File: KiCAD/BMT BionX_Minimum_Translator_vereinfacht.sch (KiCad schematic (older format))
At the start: 30 parts, among them J1 Kunteng Display Connector, J2 SAE Power Connector Motor, J3 Rosenberg Motor, J4 External BB Torquesensor, J5 Brake connector, J6 Throttle connector, J7 CAN Connector, J9 Batterieanschluß, Q1 IRF3205, Q2 IRF3205, U1 BP, U2 MCP2551-CAN Transceiver, U3 VOM1271, U4 SD12-5, U5 VOM1271

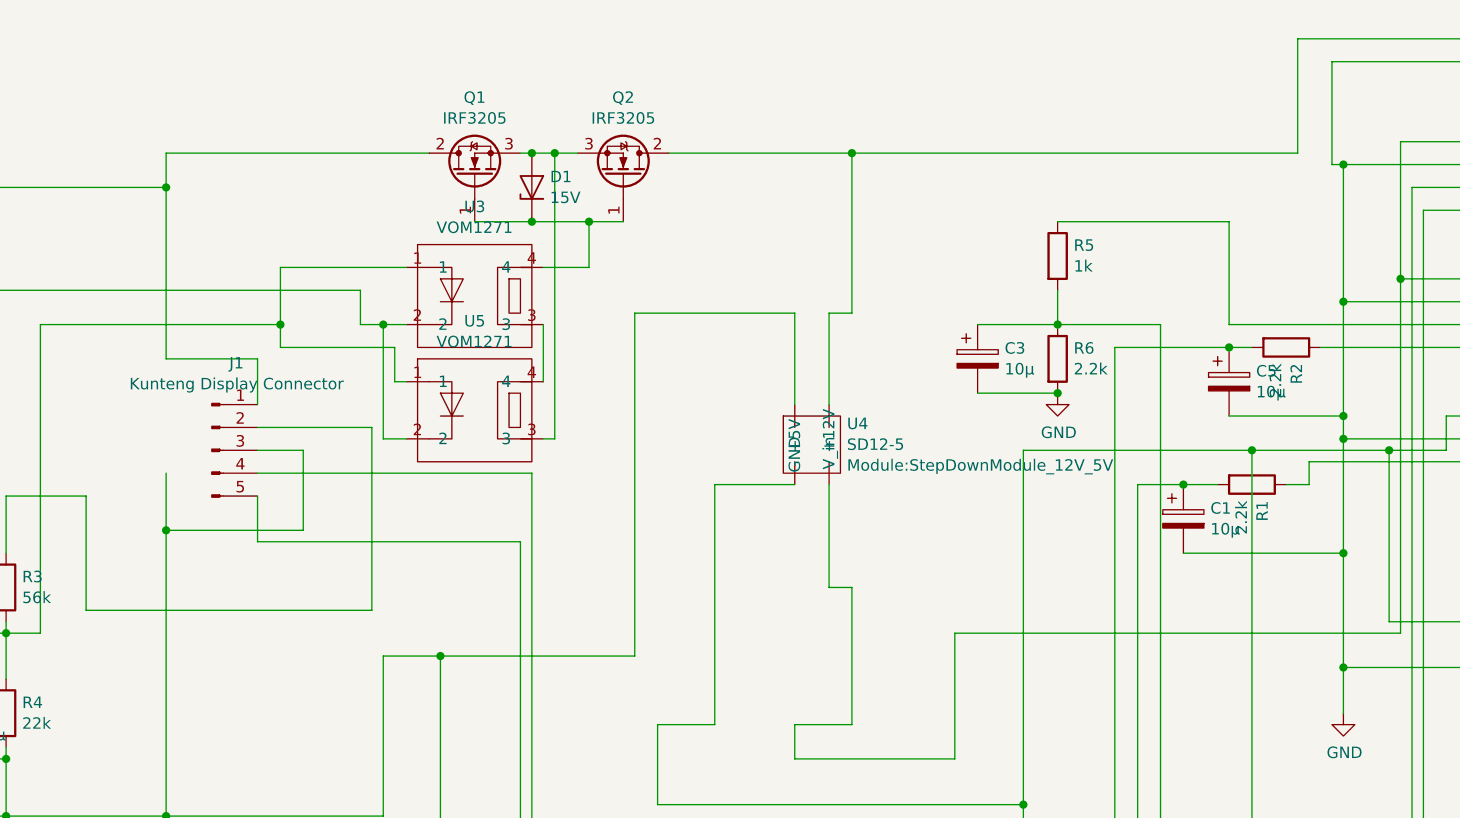
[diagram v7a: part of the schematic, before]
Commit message: Step Down switched seperately
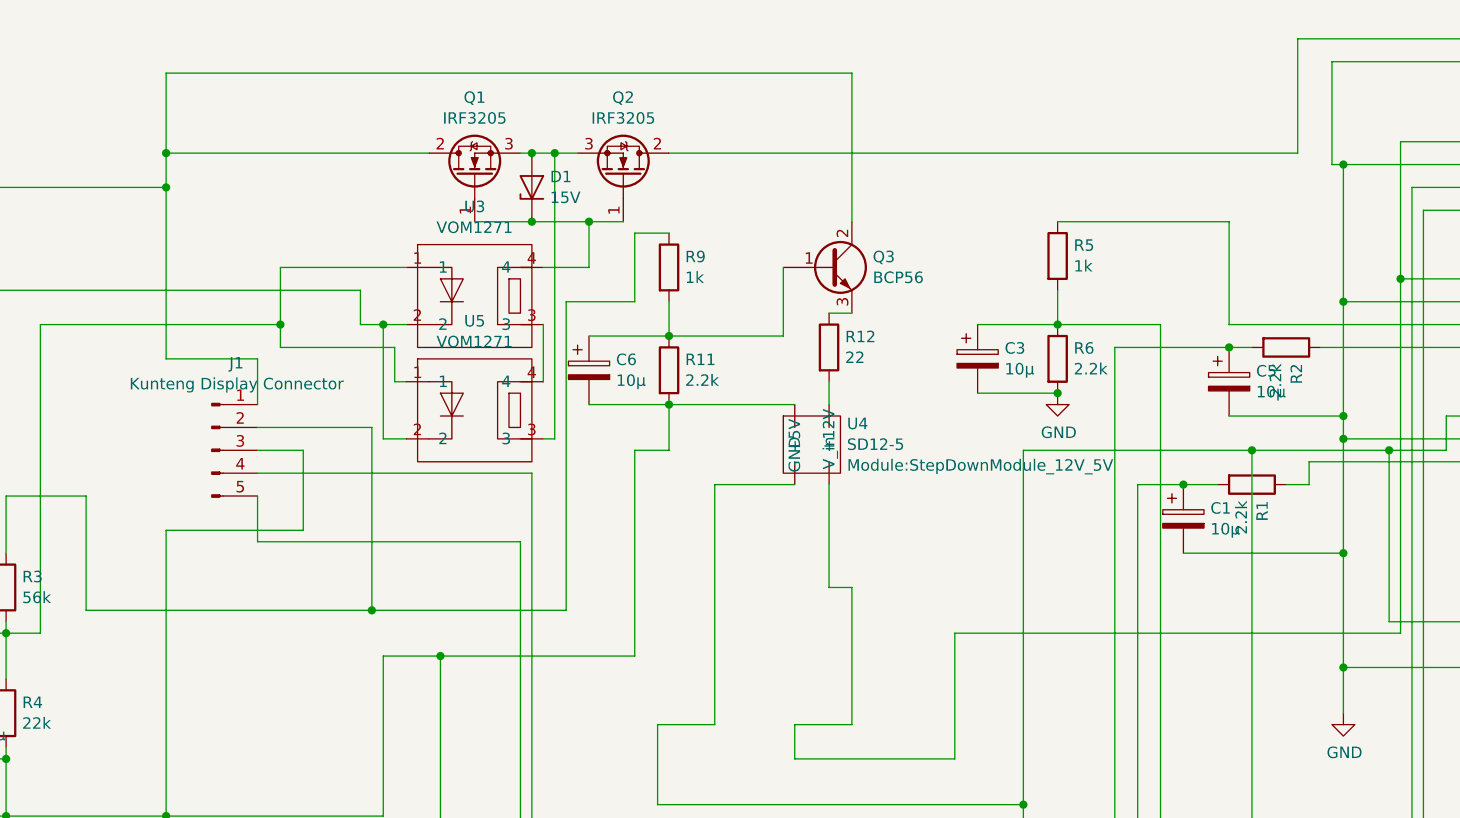
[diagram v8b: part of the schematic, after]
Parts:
- added C6: 10µ, Capacitor_THT:CP_Radial_D5.0mm_P2.50mm, symbol Device:CP
- added Q3: BCP56, Package_TO_SOT_SMD:SOT-223, symbol Transistor_BJT:BCP56
- added R11: 2.2k, Resistor_SMD:R_0805_2012Metric, symbol Device:R
- added R12: 22, Resistor_SMD:R_0805_2012Metric, symbol Device:R
- added R9: 1k, Resistor_SMD:R_0805_2012Metric, symbol Device:R
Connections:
- net +BATT: now also Q3.2 (C), Q3.4 (C)
- net GND: now also C6.2, R11.2
- net at J1.2 (Pin_2), R3.1: now also R9.1
- net at J2.1 (Pin_1), Q2.2 (D): no longer U4.V_in
- new net: C6.1, Q3.1 (B), R11.1, R9.2
- new net: Q3.3 (E), R12.1
- new net: R12.2, U4.V_in
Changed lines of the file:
@@
 $EndComp
-Wire Wire Line
-	4950 1450 5750 1450
-Connection ~ 5750 1450
-Wire Wire Line
-	5750 1450 7700 1450
-Wire Wire Line
-	5750 1450 5750 2150
 Wire Wire Line
 	6200 3550 6200 4100
@@
 Wire Wire Line
 	3950 3650 4800 3650
-Wire Wire Line
-	4800 3650 4800 2150
 Connection ~ 3950 3650
 $Comp
@@
 $EndComp
 Wire Wire Line
-	5500 2150 5500 2550
-Wire Wire Line
-	4800 2150 5500 2150
-Wire Wire Line
 	5750 2150 5650 2150
-Wire Wire Line
-	5650 2150 5650 2550
 Wire Wire Line
 	5650 2900 5650 3350
@@
 Wire Wire Line
 	3350 2750 3150 2750
-Connection ~ 2750 3100
-Wire Wire Line
-	2750 3100 2750 2850
 Wire Wire Line
 	3350 2750 3350 3100
@@
 Wire Wire Line
 	2750 1450 3900 1450
+Wire Wire Line
+	4950 1450 7700 1450
+$Comp
+L Transistor_BJT:BCP56 Q3
+U 1 1 5F8B6DF6
+P 5650 1950
+F 0 "Q3" H 5841 1996 50  0000 L CNN
+F 1 "BCP56" H 5841 1905 50  0000 L CNN
+F 2 "Package_TO_SOT_SMD:SOT-223" H 5850 1875 50  0001 L CIN
+F 3 "http://cache.nxp.com/documents/data_sheet/BCP56_BCX56_BC56PA.pdf?pspll=1" H 5650 1950 50  0001 L CNN
+	1    5650 1950
+	1    0    0    -1
+$EndComp
+Wire Wire Line
+	2750 1450 2750 1100
+Wire Wire Line
+	2750 1100 5750 1100
+Wire Wire Line
+	5750 1100 5750 1750
+Connection ~ 2750 1450
+$Comp
+L Device:R R12
+U 1 1 5F8C4819
+P 5650 2300
+F 0 "R12" H 5720 2346 50  0000 L CNN
+F 1 "22" H 5720 2255 50  0000 L CNN
+F 2 "Resistor_SMD:R_0805_2012Metric" V 5580 2300 50  0001 C CNN
+F 3 "~" H 5650 2300 50  0001 C CNN
+	1    5650 2300
+	1    0    0    -1
+$EndComp
+Wire Wire Line
+	5650 2450 5650 2550
+$Comp
+L Device:R R11
+U 1 1 5F8D30A0
+P 4950 2400
+F 0 "R11" H 5020 2446 50  0000 L CNN
+F 1 "2.2k" H 5020 2355 50  0000 L CNN
+F 2 "Resistor_SMD:R_0805_2012Metric" V 4880 2400 50  0001 C CNN
+F 3 "~" H 4950 2400 50  0001 C CNN
+	1    4950 2400
+	1    0    0    -1
+$EndComp
+Wire Wire Line
+	4950 2100 4950 2250
+Connection ~ 4950 2250
+$Comp
+L Device:CP C6
+U 1 1 5F8D30B8
+P 4600 2400
+F 0 "C6" H 4718 2446 50  0000 L CNN
+F 1 "10µ" H 4718 2355 50  0000 L CNN
+F 2 "Capacitor_THT:CP_Radial_D5.0mm_P2.50mm" H 4638 2250 50  0001 C CNN
+F 3 "~" H 4600 2400 50  0001 C CNN
+	1    4600 2400
+	1    0    0    -1
+$EndComp
+Wire Wire Line
+	4600 2250 4950 2250
+Wire Wire Line
+	4600 2550 4950 2550
+Connection ~ 4950 2550
+$Comp
+L Device:R R9
+U 1 1 5F8D30C6
+P 4950 1950
+F 0 "R9" H 5020 1996 50  0000 L CNN
+F 1 "1k" H 5020 1905 50  0000 L CNN
+F 2 "Resistor_SMD:R_0805_2012Metric" V 4880 1950 50  0001 C CNN
+F 3 "~" H 4950 1950 50  0001 C CNN
+	1    4950 1950
+	1    0    0    -1
+$EndComp
+Wire Wire Line
+	5500 2550 4950 2550
+Wire Wire Line
+	4950 2250 5450 2250
+Wire Wire Line
+	5450 2250 5450 1950
+Wire Wire Line
+	3650 3450 4500 3450
+Wire Wire Line
+	4500 3450 4500 2100
+Wire Wire Line
+	4500 2100 4800 2100
+Wire Wire Line
+	4800 2100 4800 1800
+Wire Wire Line
+	4800 1800 4950 1800
+Connection ~ 3650 3450
+Wire Wire Line
+	4800 3650 4800 2750
+Wire Wire Line
+	4800 2750 4950 2750
+Wire Wire Line
+	4950 2750 4950 2550
 $EndSCHEMATC
